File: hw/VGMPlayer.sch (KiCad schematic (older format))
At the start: 95 parts, among them J1 Micro_SD_Card, J2 EarPiece, P1 USB_C_Receptacle_16P, P2 SWD, P3 BATT, P5 ICSP, P6 CODEC, Q1 AO3401A, Q2 AO3401A, Q3 2N7002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

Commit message: Remove SD card bypass capacitor (very close to main filter cap)
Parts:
- removed C15: 10u, BZ_Capacitor:C_0603, symbol BZ_Passive:C
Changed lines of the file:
@@
 Wire Wire Line
 	5750 1400 6300 1400
-Wire Wire Line
-	6300 900  6300 850
 Text Label 5750 2000 0    40   ~ 0
 SD_DAT0
@@
 Wire Wire Line
 	6300 1500 5750 1500
-Connection ~ 6300 850
 Wire Wire Line
 	6050 1700 6300 1700
-Wire Wire Line
-	6050 850  6050 1700
-Wire Wire Line
-	6300 850  6050 850
-Wire Wire Line
-	6300 850  6300 800
-$Comp
-L BZ_Power:GND #PWR023
-U 1 1 60F50791
-P 6300 1100
-F 0 "#PWR023" H 6300 1100 30  0001 C CNN
-F 1 "GND" H 6300 1030 30  0001 C CNN
-F 2 "" H 6300 1100 60  0001 C CNN
-F 3 "" H 6300 1100 60  0001 C CNN
-	1    6300 1100
-	1    0    0    -1
-$EndComp
-$Comp
-L BZ_Passive:C C15
-U 1 1 60F244CE
-P 6300 1000
-F 0 "C15" H 6377 1038 40  0000 L CNN
-F 1 "10u" H 6377 962 40  0000 L CNN
-F 2 "BZ_Capacitor:C_0603" H 6300 1000 40  0001 C CNN
-F 3 "" H 6300 1000 40  0001 C CNN
-F 4 "GRM188R61A106KE69D " H 6300 1000 50  0001 C CNN "PN"
-F 5 "C77044" H 6300 1000 50  0001 C CNN "JLCPN"
-	1    6300 1000
-	1    0    0    -1
-$EndComp
 $Comp
 L BZ_Power:3V3 #PWR022
 U 1 1 60F23FFE
-P 6300 800
-F 0 "#PWR022" H 6300 760 40  0001 C CNN
-F 1 "3V3" H 6300 900 40  0000 C CNN
-F 2 "" H 6300 800 40  0001 C CNN
-F 3 "" H 6300 800 40  0001 C CNN
-	1    6300 800
+P 6050 850
+F 0 "#PWR022" H 6050 810 40  0001 C CNN
+F 1 "3V3" H 6050 950 40  0000 C CNN
+F 2 "" H 6050 850 40  0001 C CNN
+F 3 "" H 6050 850 40  0001 C CNN
+	1    6050 850
 	1    0    0    -1
 $EndComp
@@
 Wire Wire Line
 	1300 2650 2200 2650
+Wire Wire Line
+	6050 850  6050 1700
 $EndSCHEMATC

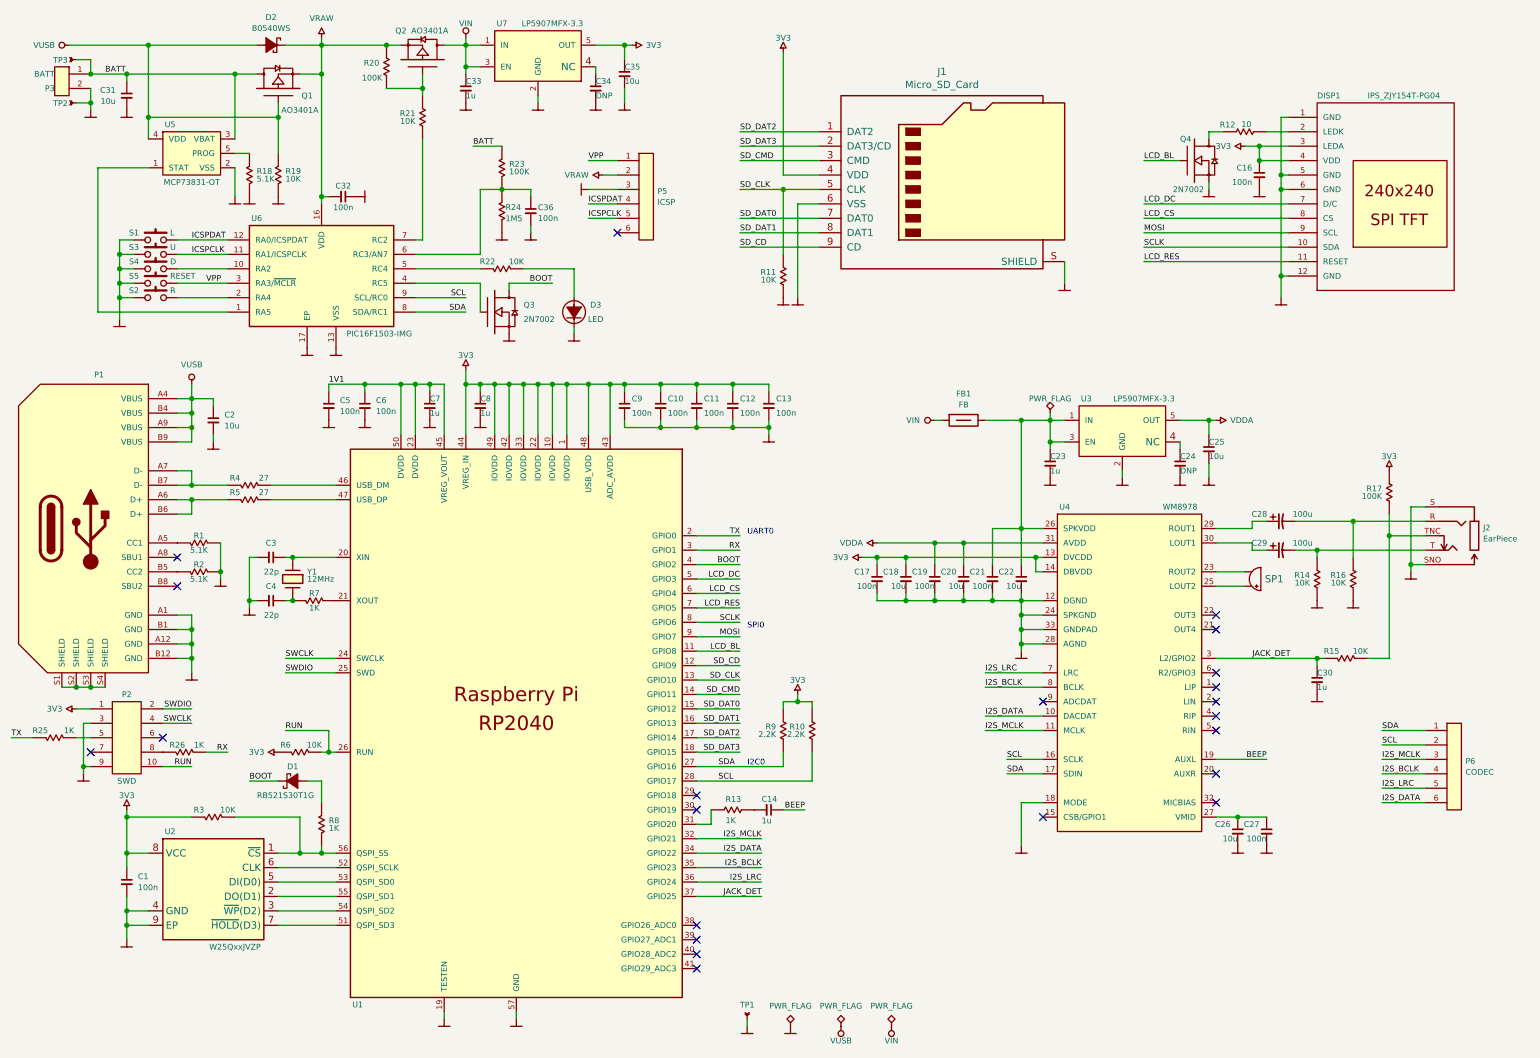
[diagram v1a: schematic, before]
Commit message: Add analog power selection jumper and multiple button options
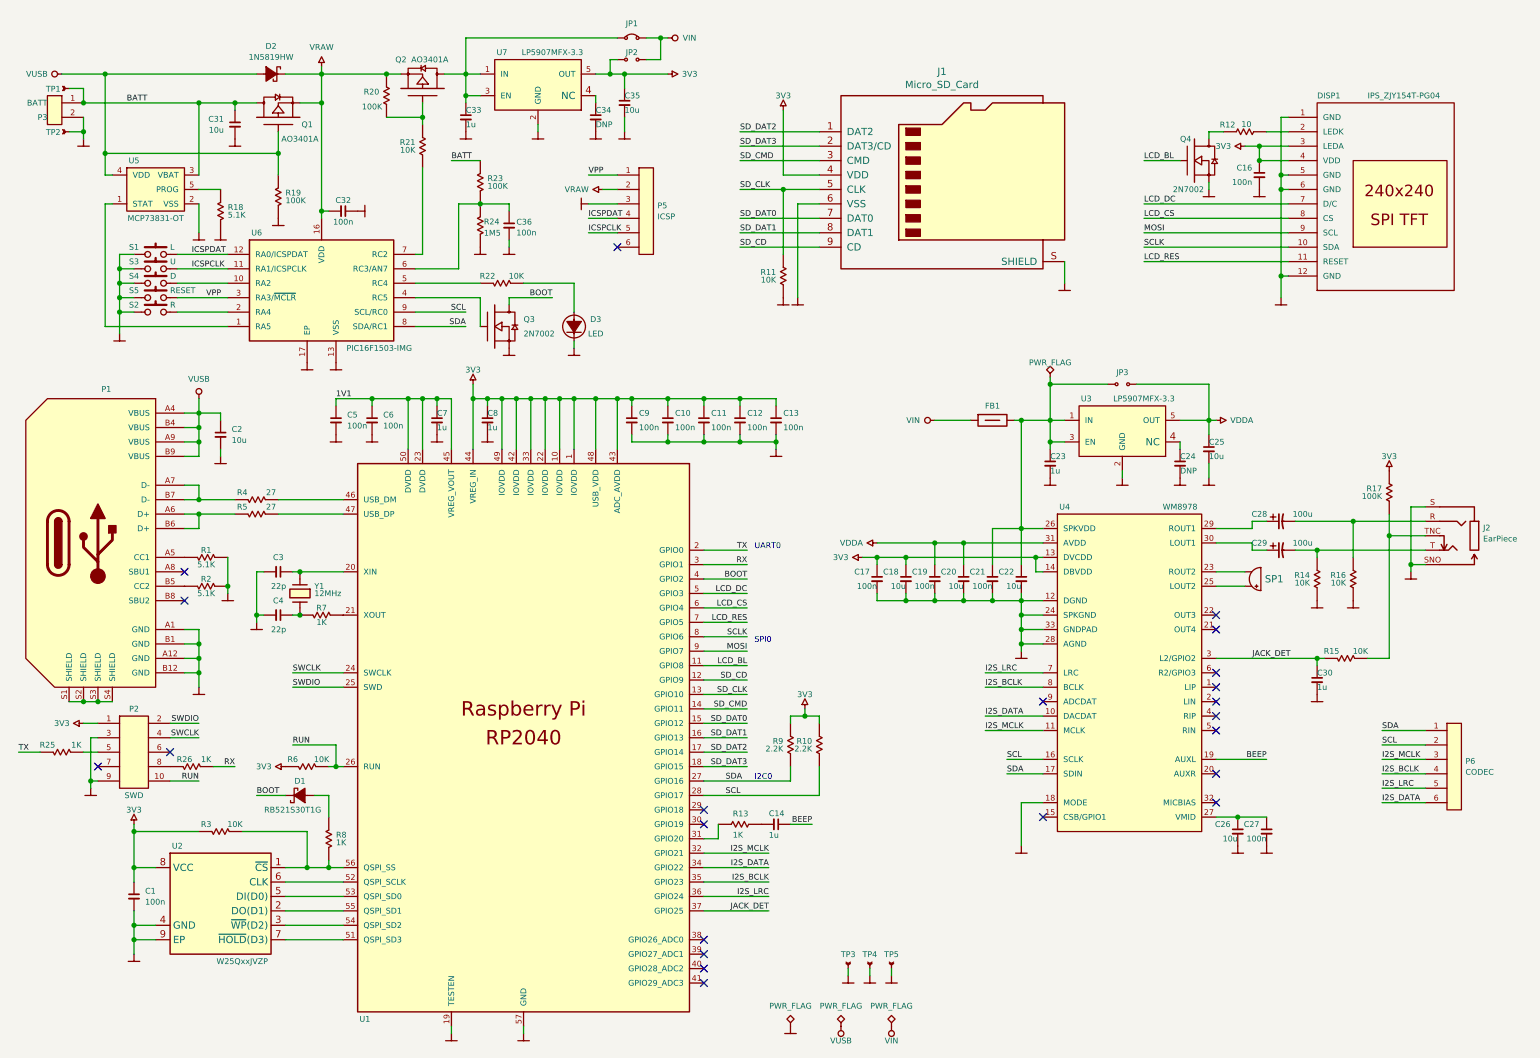
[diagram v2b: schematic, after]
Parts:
- added JP1: Jumper-NC, BZ_Misc:Jumper-Solder, symbol BZ_Misc:Jumper-NC
- added JP2, JP3: Jumper-NO, BZ_Misc:Jumper-Solder, symbol BZ_Misc:Jumper-NO
- added TP3, TP4: TP, BZ_Misc:TP_THT-Pad-0.8, symbol BZ_Misc:TP
- D2: value B0540WS -> 1N5819HW; footprint BZ_Diode:D_SOD-323 -> BZ_Diode:D_SOD-123
- R19: value 10K -> 100K
- S1, S2, S3, S4: footprint BZ_Switch:C&K_PTS525 -> VGMPlayer:MultiButton
- S5: footprint BZ_Switch:SW-PUSH_3x2x0.6H -> BZ_Switch:SW-PUSH_4x3x2H
- renumbered TP3 to TP1, TP1 to TP5
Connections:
- net 3V3: now also JP2.1
- net GND: now also TP3.1, TP4.1
- net VDDA: now also JP3.2
- net VIN: now also JP1.2, JP2.2; no longer C33.1, Q2.3 (D), U7.1 (IN), U7.3 (EN)
- net at C21.1, C22.1, C23.1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: now also JP3.1
- new net: C33.1, JP1.1, Q2.3 (D), U7.1 (IN), U7.3 (EN)
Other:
- moved on the sheet: C1, C10, C11, C12, C13, C14, C2, C3, C31, C32, C33, C34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

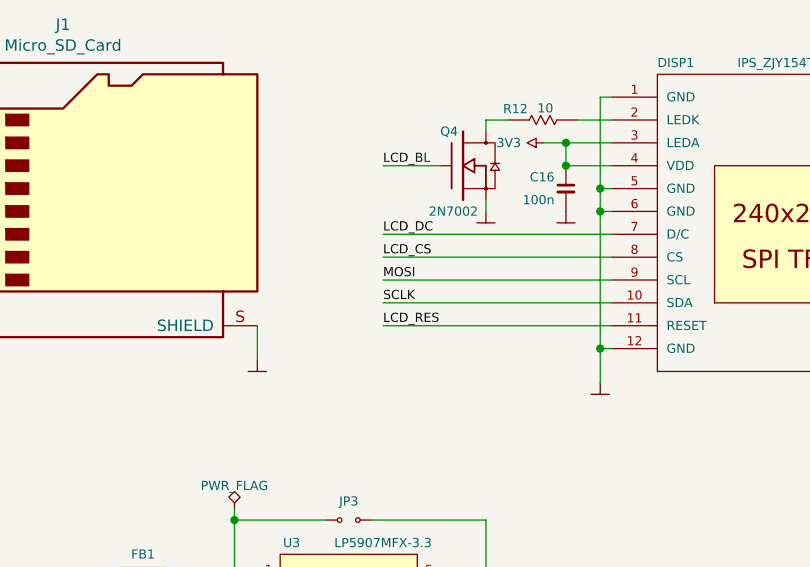
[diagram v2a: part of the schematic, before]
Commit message: Fix LCD wiring
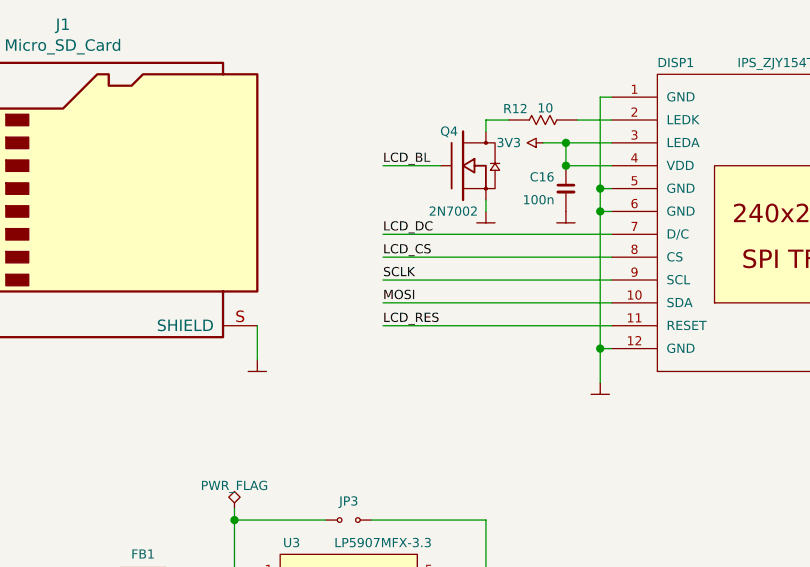
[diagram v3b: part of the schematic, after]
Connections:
- net MOSI: now also DISP1.10 (SDA); no longer DISP1.9 (SCL)
- net SCLK: now also DISP1.9 (SCL); no longer DISP1.10 (SDA)
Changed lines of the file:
@@
 Text Label 8550 2000 0    40   ~ 0
 LCD_CS
+Text Label 8550 2200 0    40   ~ 0
+MOSI
 Text Label 8550 2100 0    40   ~ 0
-MOSI
-Text Label 8550 2200 0    40   ~ 0
 SCLK
 Text Label 8550 2300 0    40   ~ 0

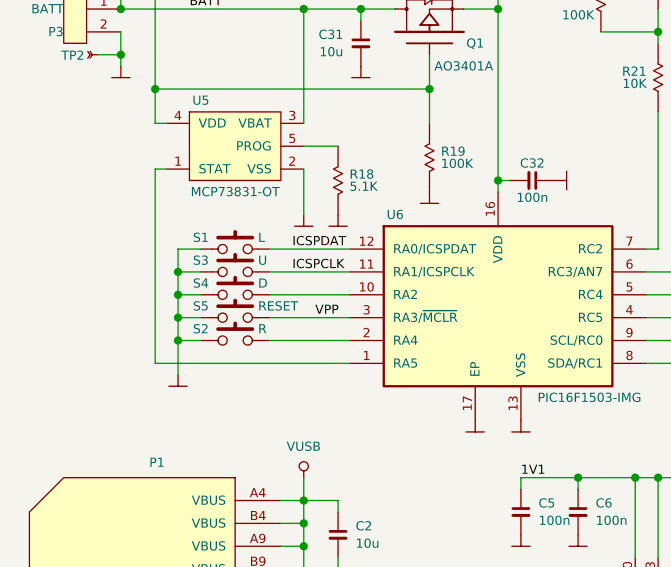
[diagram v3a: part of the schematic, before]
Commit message: Rename button labels
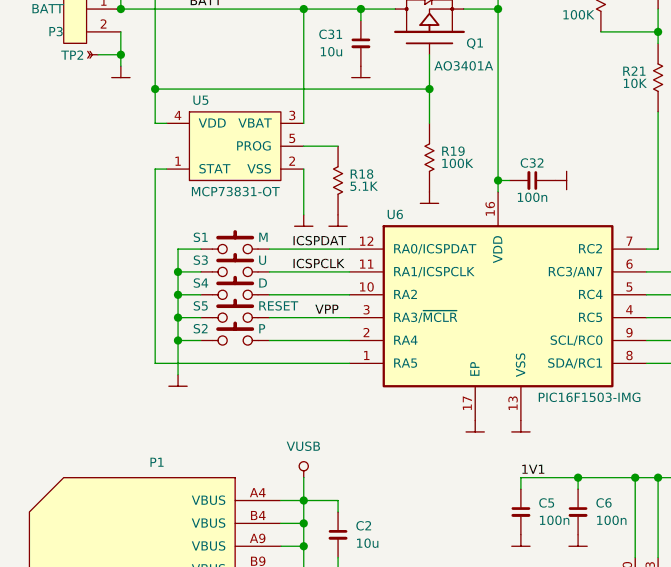
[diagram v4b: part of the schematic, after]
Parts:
- S1: value L -> M
- S2: value R -> P
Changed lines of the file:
@@
 P 1700 2250
 F 0 "S1" H 1550 2300 40  0000 C CNN
-F 1 "L" H 1800 2300 40  0000 L CNN
+F 1 "M" H 1800 2300 40  0000 L CNN
 F 2 "VGMPlayer:MultiButton" H 1700 2250 40  0001 C CNN
 F 3 "" H 1700 2250 40  0001 C CNN
@@
 P 1700 2650
 F 0 "S2" H 1550 2700 40  0000 C CNN
-F 1 "R" H 1800 2700 40  0000 L CNN
+F 1 "P" H 1800 2700 40  0000 L CNN
 F 2 "VGMPlayer:MultiButton" H 1700 2650 40  0001 C CNN
 F 3 "" H 1700 2650 40  0001 C CNN
